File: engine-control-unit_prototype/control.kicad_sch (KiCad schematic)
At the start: 33 parts, among them J24 HEATER_IPA, J25 HEATER_NOS, J26 VALVE_IPA, J27 VALVE_NOS, J28 NOS ENCODER, J30 IPA ENCODER, J31 VCTR_CONN, Q2 NMOS, Q3 NMOS, Q4 NPN, Q5 NPN, Q6 NPN

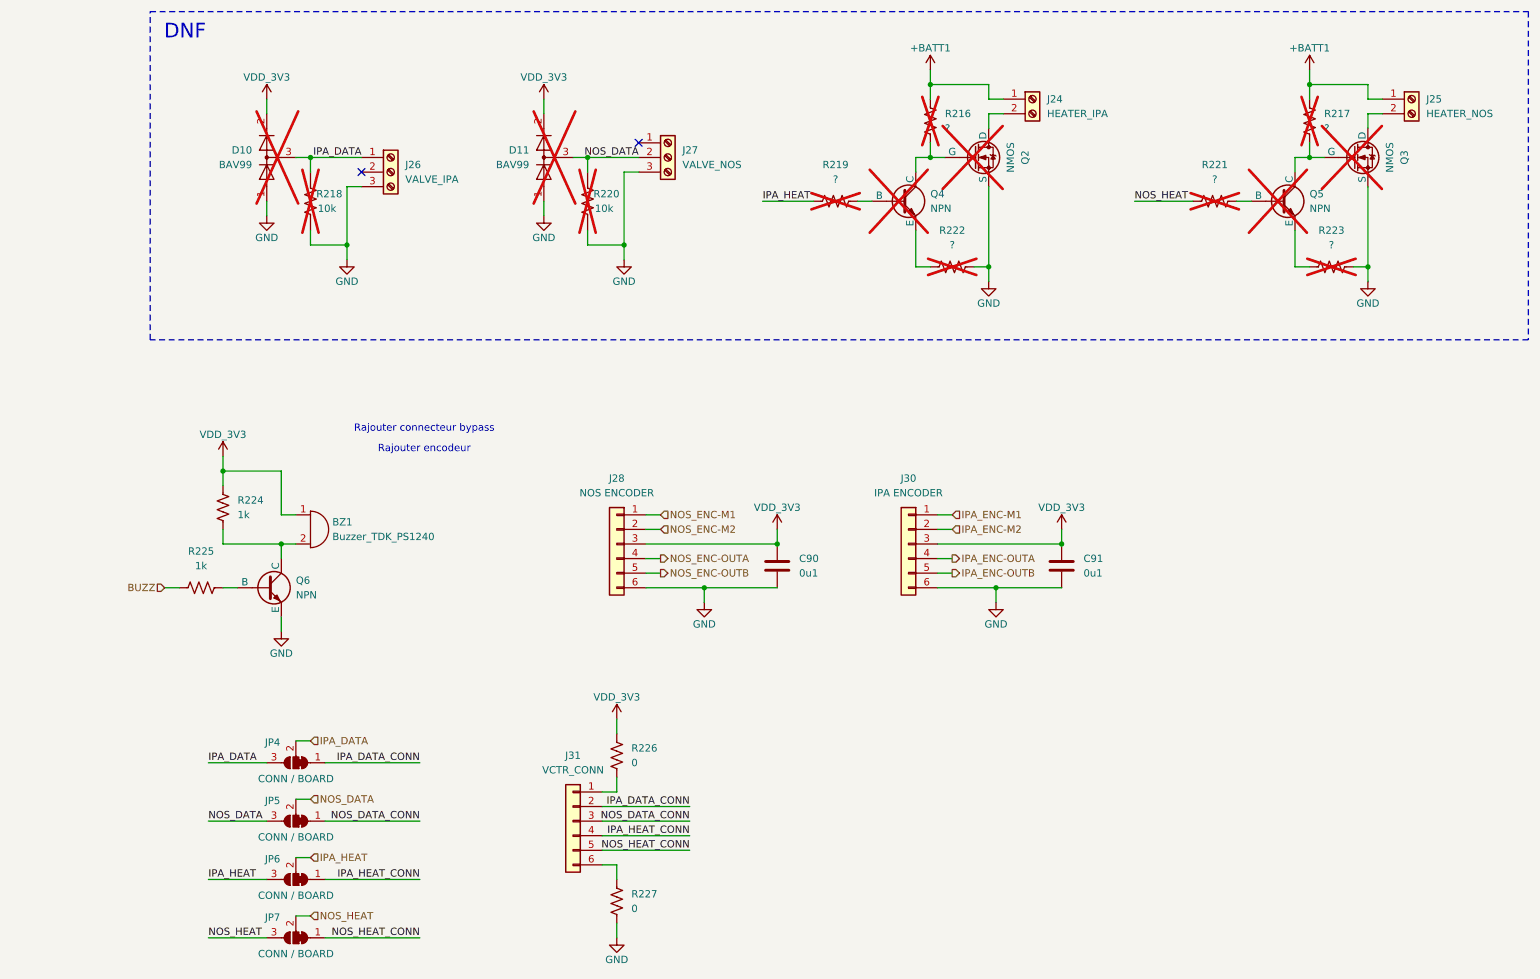
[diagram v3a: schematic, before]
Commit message: ajout de page root
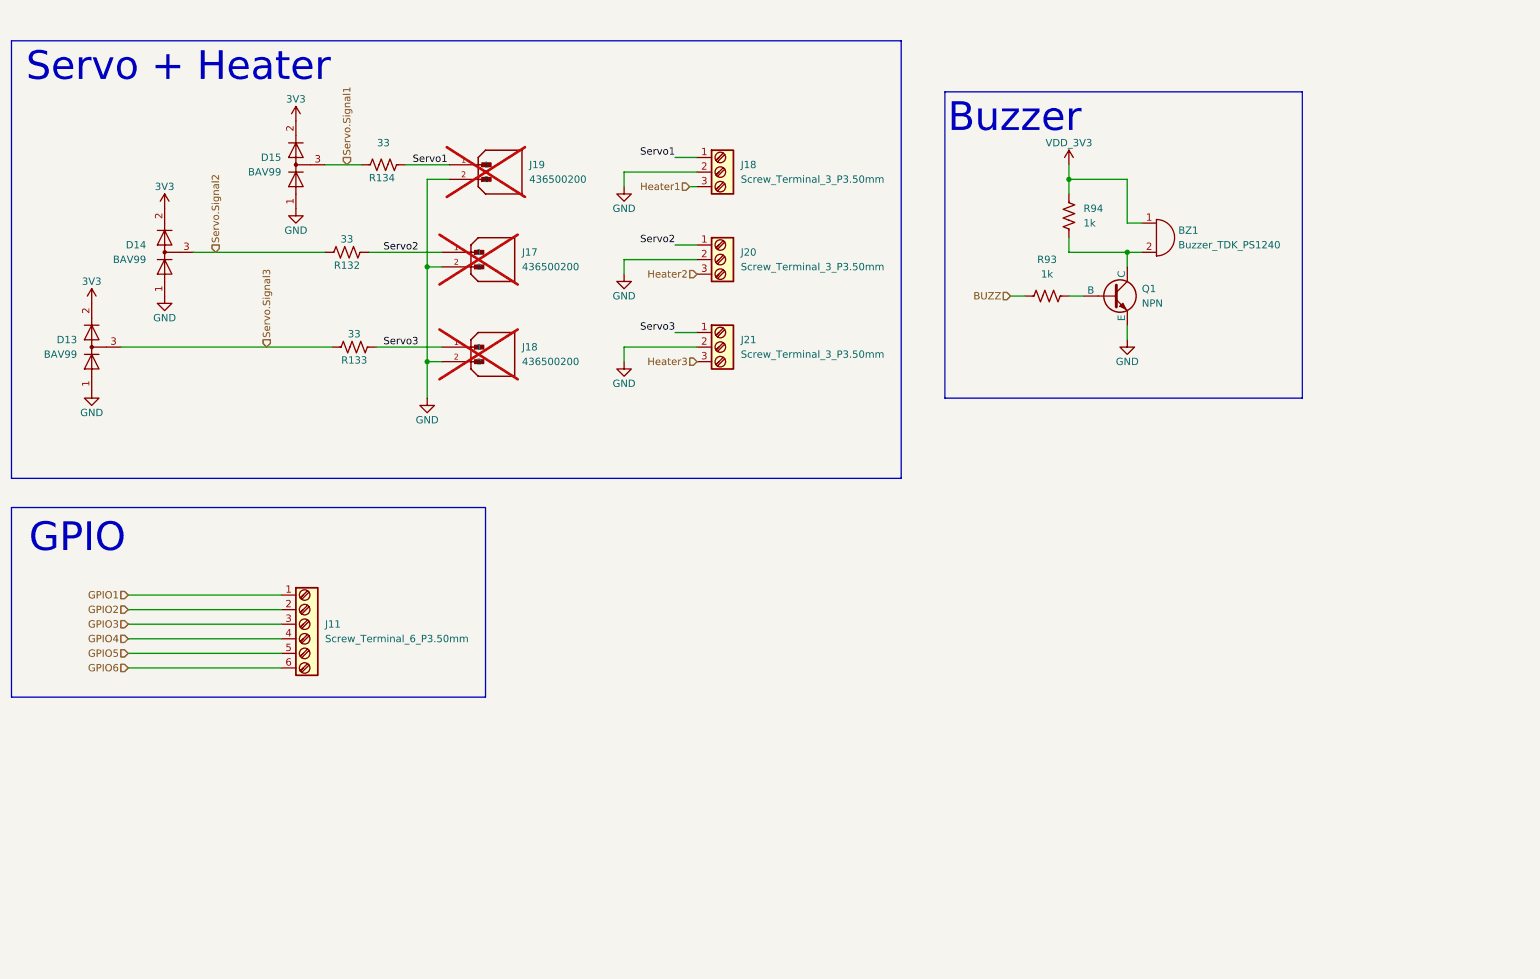
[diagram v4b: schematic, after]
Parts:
- removed C90, C91: 0u1, Capacitor_SMD:C_0402_1005Metric, symbol Device:C
- removed D10, D11: BAV99, Package_TO_SOT_SMD:SOT-23, symbol Diode:BAV99
- removed J24: HEATER_IPA, Connector_PinSocket_2.54mm:PinSocket_1x02_P2.54mm_Vertical, symbol Connector:Screw_Terminal_01x02
- removed J25: HEATER_NOS, Connector_PinSocket_2.54mm:PinSocket_1x02_P2.54mm_Vertical, symbol Connector:Screw_Terminal_01x02
- removed J26: VALVE_IPA, Connector_PinSocket_2.54mm:PinSocket_1x03_P2.54mm_Vertical, symbol Connector:Screw_Terminal_01x03
- removed J27: VALVE_NOS, Connector_PinSocket_2.54mm:PinSocket_1x03_P2.54mm_Vertical, symbol Connector:Screw_Terminal_01x03
- removed J28: NOS ENCODER, Connector_PinSocket_2.54mm:PinSocket_1x06_P2.54mm_Vertical, symbol Connector_Generic:Conn_01x06
- removed J30: IPA ENCODER, Connector_PinSocket_2.54mm:PinSocket_1x06_P2.54mm_Vertical, symbol Connector_Generic:Conn_01x06
- removed J31: VCTR_CONN, Connector_PinSocket_2.54mm:PinSocket_1x06_P2.54mm_Vertical, symbol Connector_Generic:Conn_01x06
- removed JP4, JP5, JP6, JP7: CONN / BOARD, Jumper:SolderJumper-3_P1.3mm_Bridged12_RoundedPad1.0x1.5mm, symbol Jumper:SolderJumper_3_Bridged12
- removed Q2, Q3: NMOS, symbol Simulation_SPICE:NMOS
- removed Q4, Q5: NPN, symbol Simulation_SPICE:NPN
- removed R216, R217, R219, R221, R222, R223: ?, Resistor_SMD:R_0603_1608Metric, symbol Device:R_US
- removed R218, R220: 10k, Resistor_SMD:R_0603_1608Metric_Pad0.98x0.95mm_HandSolder, symbol 0CSL_D1_V1:RES0603
- removed R226, R227: 0, Resistor_SMD:R_0201_0603Metric, symbol Device:R_US
- added D13, D14, D15: BAV99, Package_TO_SOT_SMD:SOT-23, symbol Diode:BAV99
- added J11: Screw_Terminal_6_P3.50mm, TerminalBlock_Phoenix:TerminalBlock_Phoenix_PT-1,5-6-3.5-H_1x06_P3.50mm_Horizontal, symbol PCM_SL_Screw_Terminal:Screw_Terminal_6_P3.50mm
- added J17, J18, J19: 436500200, MOLEX:MOLEX_436500200, symbol MOLEX:436500200
- added J18, J20, J21: Screw_Terminal_3_P3.50mm, TerminalBlock_Phoenix:TerminalBlock_Phoenix_PT-1,5-3-3.5-H_1x03_P3.50mm_Horizontal, symbol PCM_SL_Screw_Terminal:Screw_Terminal_3_P3.50mm
- added R132, R133, R134: 33, Capacitor_SMD:C_0603_1608Metric, symbol Device:R_US
- BZ1: footprint 0CSL_D1_V1:Buzzer_TDK_PS1240P02BT_D12.2mmP5mm -> Buzzer_Beeper:Buzzer_Murata_PKMCS0909E; Cost $0.91 -> (none); Digikey (none) -> https://www.digikey.ca/en/products/detail/murata-electronic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; Manufacturer Part Number PS1240P02BT -> (none); Mfg #1 TDK Corporation -> (none); No Digikey 445-2525-1-ND -> (none); Projet PR4_2022 Andre pour Sandrine Lacroix-Pierre -> (none); Projet Prealable Mod de la lib KiKad -> (none)
- renumbered Q6 to Q1, R225 to R93, R224 to R94
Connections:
- net GND: now also D13.1 (K), D14.1 (K), D15.1 (K), J17.2, J18.2, J18.2, J19.2, J20.2, J21.2
- new net 3V3: D13.2 (A), D14.2 (A), D15.2 (A)
- new net GPIO1: J11.1
- new net GPIO2: J11.2
- new net GPIO3: J11.3
- new net GPIO4: J11.4
- new net GPIO5: J11.5
- new net GPIO6: J11.6
- new net Heater1: J18.3
- new net Heater2: J20.3
- new net Heater3: J21.3
- new net Servo.Signal1: D15.3 (K), R134.1
- new net Servo.Signal2: D14.3 (K), R132.2
- new net Servo.Signal3: D13.3 (K), R133.2
- new net Servo1: J18.1, J19.1, R134.2
- new net Servo2: J17.1, J20.1, R132.1
- new net Servo3: J18.1, J21.1, R133.1
- no-connect marks 2 -> 0
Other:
- note added: "Buzzer"
- note added: "GPIO"
- note added: "Servo + Heater"
- note removed: "DNF"
- note removed: "Rajouter connecteur bypass"
- note removed: "Rajouter encodeur"
- moved on the sheet: BZ1, Q1, R93, R94
